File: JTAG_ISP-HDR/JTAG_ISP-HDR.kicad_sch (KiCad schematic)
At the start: 4 parts, among them J1 Conn_01x08, J2 Conn_01x08

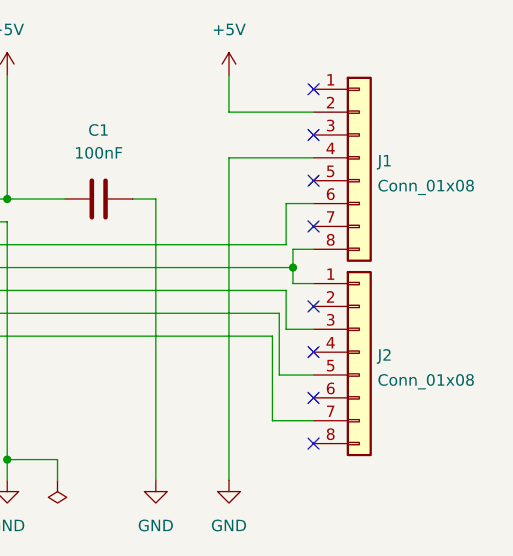
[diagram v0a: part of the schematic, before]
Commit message: # [PCB] ~ Modification du PCB pour le projet ISP en fonction des nouvelles connexions sur son schéma. + Ajout de trous aux 4 coins du PCB des 2 projets (ISP & HDR). ~ Augmentation de la taille du PCB des 2 projets en ajoutant 20mills en haut et en bas. ~ Diminution de l'espace de texte (nom et date).
# [SCHÉMA]
~ Modification du schéma pour le projet ISP basé sur le fil JTAG -> ISP déjà existant.
+ Ajout de texte sur le schéma des 2 projets indiquant le nom des broches sur les headers.
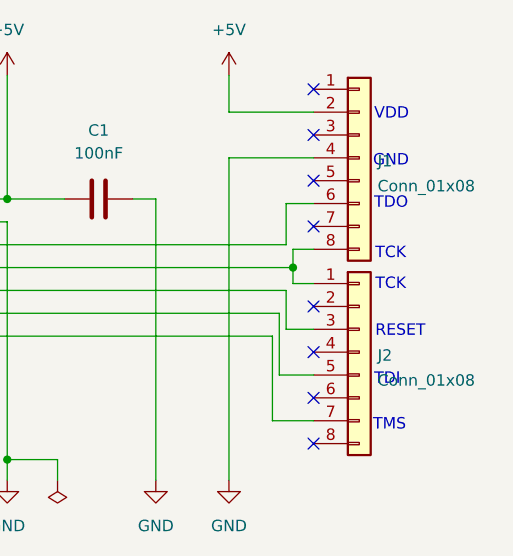
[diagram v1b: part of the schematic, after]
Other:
- note added: "GND"
- note added: "RESET"
- note added: "TCK"
- note added: "TDI"
- note added: "TDO"
- note added: "TMS"
- note added: "VDD"
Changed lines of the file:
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@@
     (stroke (width 0) (type default) (color 0 0 0 0))
+  )
+  (text "TDI" (at 181.483 108.712 0)
+    (effects (font (size 1.27 1.27)) (justify left bottom))
+  )
+  (text "TMS" (at 181.356 113.792 0)
+    (effects (font (size 1.27 1.27)) (justify left bottom))
+  )
+  (text "GND" (at 181.356 84.455 0)
+    (effects (font (size 1.27 1.27)) (justify left bottom))
+  )
+  (text "TCK" (at 181.61 94.742 0)
+    (effects (font (size 1.27 1.27)) (justify left bottom))
+  )
+  (text "TCK" (at 181.61 98.171 0)
+    (effects (font (size 1.27 1.27)) (justify left bottom))
+  )
+  (text "VDD" (at 181.483 79.248 0)
+    (effects (font (size 1.27 1.27)) (justify left bottom))
+  )
+  (text "RESET" (at 181.61 103.378 0)
+    (effects (font (size 1.27 1.27)) (justify left bottom))
+  )
+  (text "TDO" (at 181.483 89.154 0)
+    (effects (font (size 1.27 1.27)) (justify left bottom))
   )
   (symbol (lib_id "power:PWR_FLAG") (at 146.304 119.126 180) (unit 1)

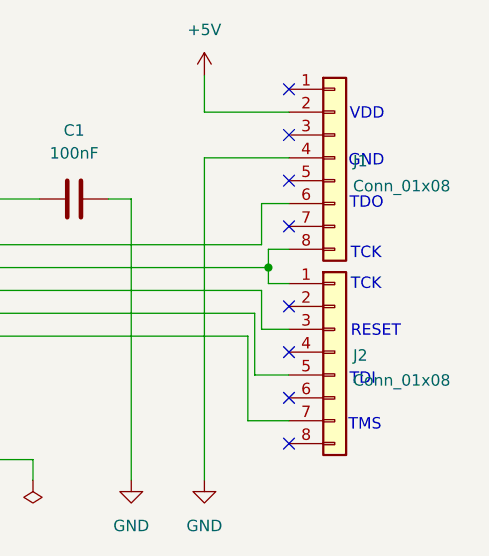
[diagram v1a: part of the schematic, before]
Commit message: # [PCB] ~ Modification du texte (date du jour) sur le PCB du projet HDR.
# [SCHÉMA]
~ Alignement du texte sur le schéma des 2 projets indiquant le nom des broches sur les headers.
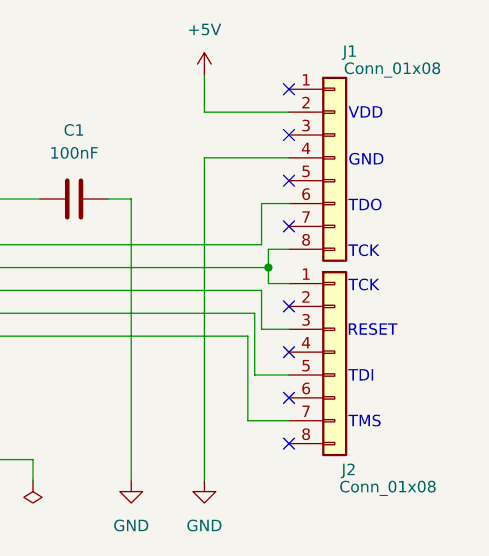
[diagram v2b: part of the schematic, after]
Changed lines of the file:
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@@
     (stroke (width 0) (type default) (color 0 0 0 0))
   )
-  (text "TDI" (at 181.483 108.712 0)
+  (text "TDI" (at 181.356 108.458 0)
     (effects (font (size 1.27 1.27)) (justify left bottom))
   )
-  (text "TMS" (at 181.356 113.792 0)
+  (text "TMS" (at 181.356 113.538 0)
     (effects (font (size 1.27 1.27)) (justify left bottom))
   )
@@
     (effects (font (size 1.27 1.27)) (justify left bottom))
   )
-  (text "TCK" (at 181.61 94.742 0)
+  (text "TCK" (at 181.356 94.615 0)
     (effects (font (size 1.27 1.27)) (justify left bottom))
   )
-  (text "TCK" (at 181.61 98.171 0)
+  (text "TCK" (at 181.356 98.425 0)
     (effects (font (size 1.27 1.27)) (justify left bottom))
   )
-  (text "VDD" (at 181.483 79.248 0)
+  (text "VDD" (at 181.356 79.248 0)
     (effects (font (size 1.27 1.27)) (justify left bottom))
   )
-  (text "RESET" (at 181.61 103.378 0)
+  (text "RESET" (at 181.229 103.378 0)
     (effects (font (size 1.27 1.27)) (justify left bottom))
   )
-  (text "TDO" (at 181.483 89.154 0)
+  (text "TDO" (at 181.356 89.535 0)
     (effects (font (size 1.27 1.27)) (justify left bottom))
   )
@@
   )
   (symbol (lib_id "Connector_Generic:Conn_01x08") (at 179.832 83.312 0) (unit 1)
-    (in_bom yes) (on_board yes) (fields_autoplaced)
-    (property "Reference" "J1" (id 0) (at 181.864 83.6735 0)
+    (in_bom yes) (on_board yes)
+    (property "Reference" "J1" (id 0) (at 180.721 71.501 0)
       (effects (font (size 1.27 1.27)) (justify left))
     )
-    (property "Value" "Conn_01x08" (id 1) (at 181.864 86.4486 0)
+    (property "Value" "Conn_01x08" (id 1) (at 180.848 73.406 0)
       (effects (font (size 1.27 1.27)) (justify left))
     )
@@
   )
   (symbol (lib_id "Connector_Generic:Conn_01x08") (at 179.832 104.902 0) (unit 1)
-    (in_bom yes) (on_board yes) (fields_autoplaced)
-    (property "Reference" "J2" (id 0) (at 181.864 105.2635 0)
+    (in_bom yes) (on_board yes)
+    (property "Reference" "J2" (id 0) (at 180.594 117.983 0)
       (effects (font (size 1.27 1.27)) (justify left))
     )
-    (property "Value" "Conn_01x08" (id 1) (at 181.864 108.0386 0)
+    (property "Value" "Conn_01x08" (id 1) (at 180.34 119.888 0)
       (effects (font (size 1.27 1.27)) (justify left))
     )

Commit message: # [PCB] + Ajout d'un encavure dans le haut du PCB du projet HDR pour que la dragone ne dépasse pas sur le bord du PCB. - Suppression du fichier .round-tracks-config qui est inutile. * Mise à jours de la cartouche pour les 2 projets.     * Date actuelle.     * Version actuelle.     * Titre du projet.
# [SCHÉMA]
* Mise à jours de la cartouche pour les 2 projets.
    * Date actuelle.
    * Version actuelle.
    * Titre du projet.
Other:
- title: JTAG_ISP -> JTAG_ISP / HDR
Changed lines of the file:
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@@
   (paper "A4")
   (title_block
-    (title "JTAG_ISP")
-    (date "2022-03-12")
-    (rev "v1.0.0")
+    (title "JTAG_ISP / HDR")
+    (date "2022-03-17")
+    (rev "v4.1.0")
   )
   (junction (at 172.466 95.504) (diameter 0) (color 0 0 0 0)

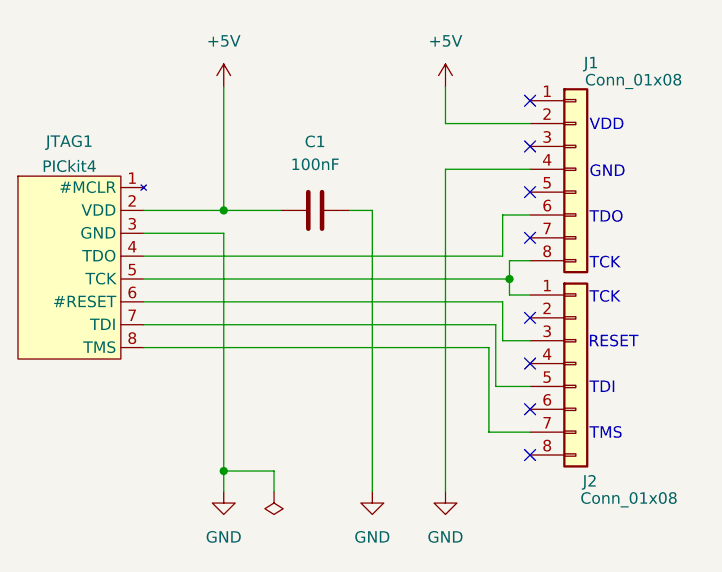
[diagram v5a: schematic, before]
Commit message: # [PCB] + Ajout de GND et de VCC dans le projet HDR sur les broches non utilisés de J1 & J2.     + Ajout des nouveaux vias. * Projet HDR routé à nouveau. * Utilisation de trous de montage avec pads. * Flèche d'indication de la broche #1 pour le PICKit4 dans le projet HDR est déplacée pour s'alligner avec celle sur le PICKit4. * Modification du texte (initiales et date du jour) sur le PCB du projet HDR.
# [SCHÉMA]
+ Ajout de GND et de VCC dans le projet HDR sur les broches non utilisées de J1 & J2.
    + Ajout des nouveaux noms de broches sur J1 & J2.
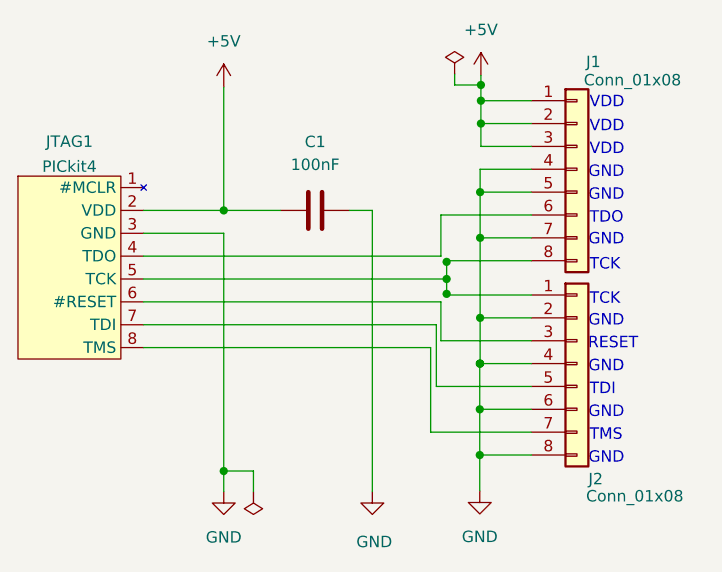
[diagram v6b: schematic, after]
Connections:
- net +5V: now also J1.1 (Pin_1), J1.3 (Pin_3)
- net GND: now also J1.5 (Pin_5), J1.7 (Pin_7), J2.2 (Pin_2), J2.4 (Pin_4), J2.6 (Pin_6), J2.8 (Pin_8)
- no-connect marks 8 -> 0

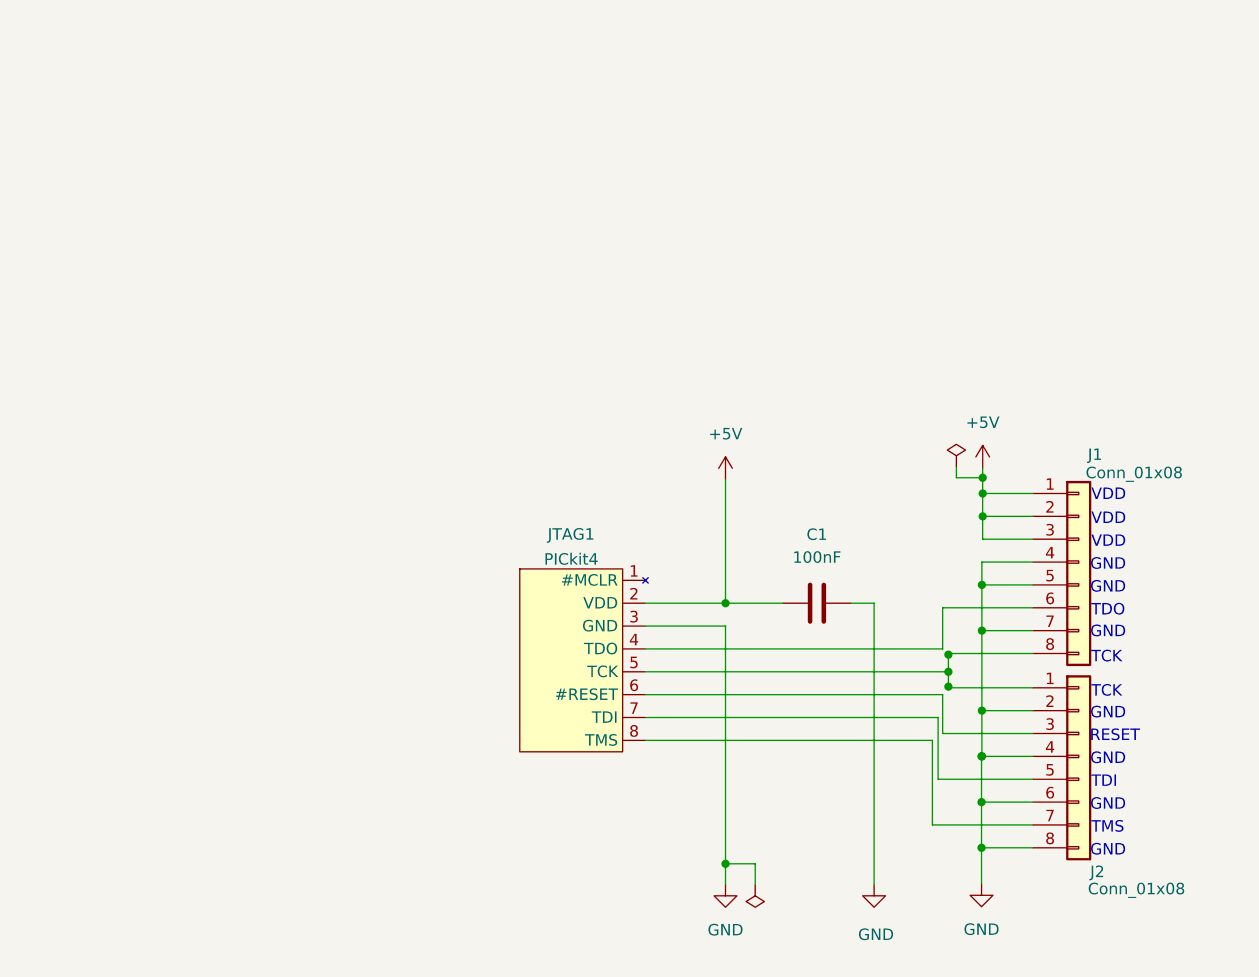
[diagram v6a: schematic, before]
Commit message: # Version compacte en cours... ## Les headers passent à travers d'un PCB et dépassent moins que la version précédente.
# [PCB]
+ Ajout d'un trou pour l'ISP dans le PCB du projet HDR.
+ Ajout d'un trou pour le PICkit dans le PCB du projet ISP.
* Déplacement du circuit de DEL dans le projet HDR.
* Projet ISP routé à nouveau.
* Mise à jour de la cartouche pour les 2 projets.
    * Date actuelle;
    * Version actuelle;

# [SCHÉMA]
+ Ajout d'encadrés pointillés dan les 2 projets pour séparer les parties du schémas.
* Déplacement du circuit de DEL dans le projet HDR.
* Réduction de la valeur de la résistance pour le circuit de DEL.
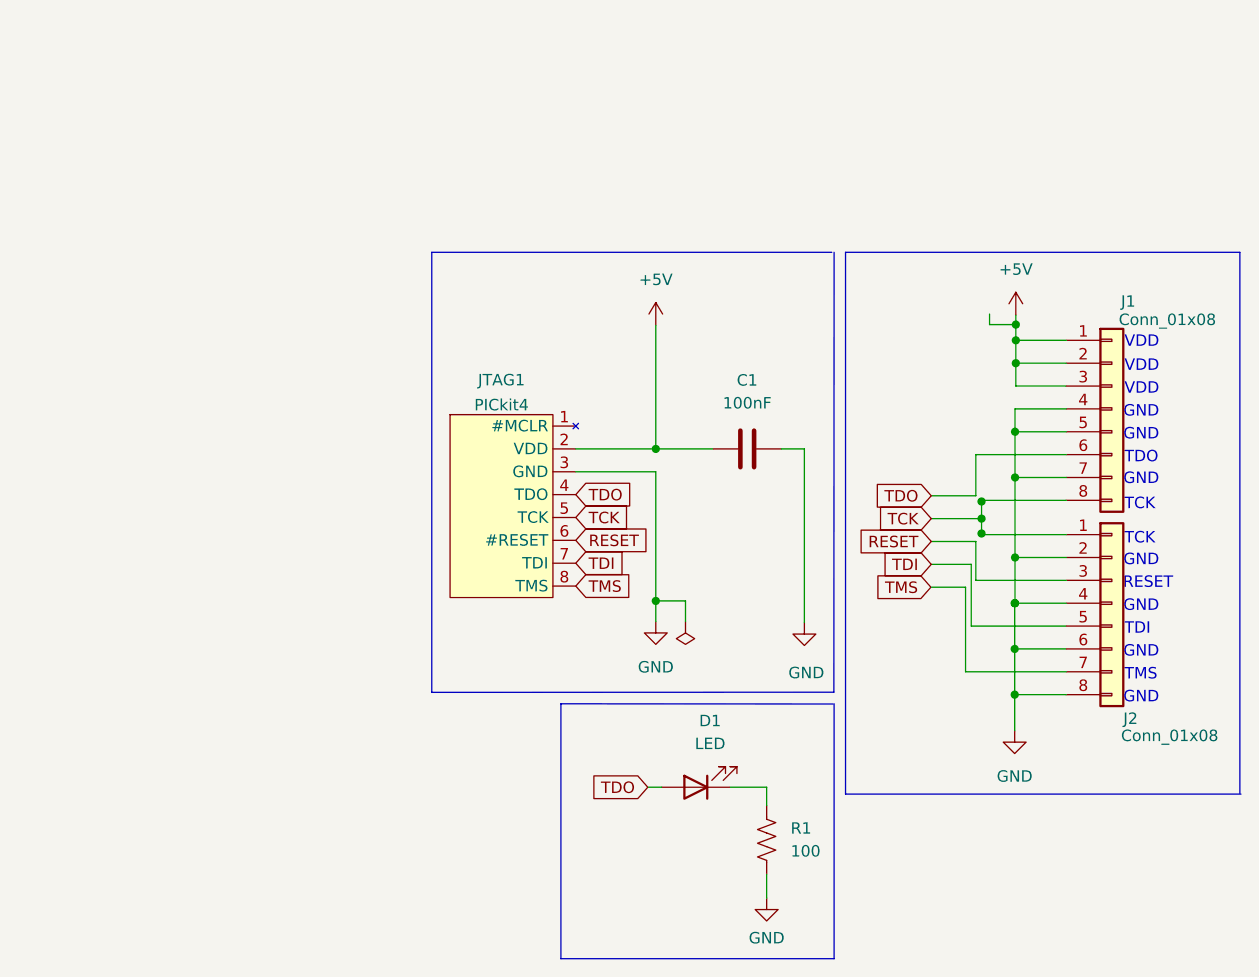
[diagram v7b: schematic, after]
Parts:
- added D1: LED, LED_THT:LED_D3.0mm, symbol Device:LED
- added R1: 100, Resistor_THT:R_Axial_DIN0207_L6.3mm_D2.5mm_P10.16mm_Horizontal, symbol Device:R_US
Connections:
- net GND: now also R1.2
- net TDO: now reaches J1.6 (Pin_6), JTAG1.4 (TDO)
- net TDO: now also D1.2 (A)
- net TCK: now reaches J1.8 (Pin_8), J2.1 (Pin_1), JTAG1.5 (TCK)
- net RESET: now reaches J2.3 (Pin_3), JTAG1.6 (#RESET)
- net TDI: now reaches J2.5 (Pin_5), JTAG1.7 (TDI)
- net TMS: now reaches J2.7 (Pin_7), JTAG1.8 (TMS)
- new net: D1.1 (K), R1.1
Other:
- moved on the sheet: J1, J2

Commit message: # [PCB] + Ajout du dégagement de 40 mils sur la bordure du trou au centre du PCB et sur le pourtour. + Ajout de la flèche indiquand la broche #1 du header du ISP. + Double vias pour les traces d'alimentation. - Suppression du texte (date du jour) dans le bas du PCB. - Suppression de la flèche indiquand la broche #1 du header PICkit4. * Nouveau format de page A5. * PCB routé à nouveau. * Mise à jour de la cartouche.     * Date actuelle;     * Version actuelle.
# [SCHÉMA]
* Mise à jour de la cartouche.
    * Date actuelle;
    * Version actuelle.
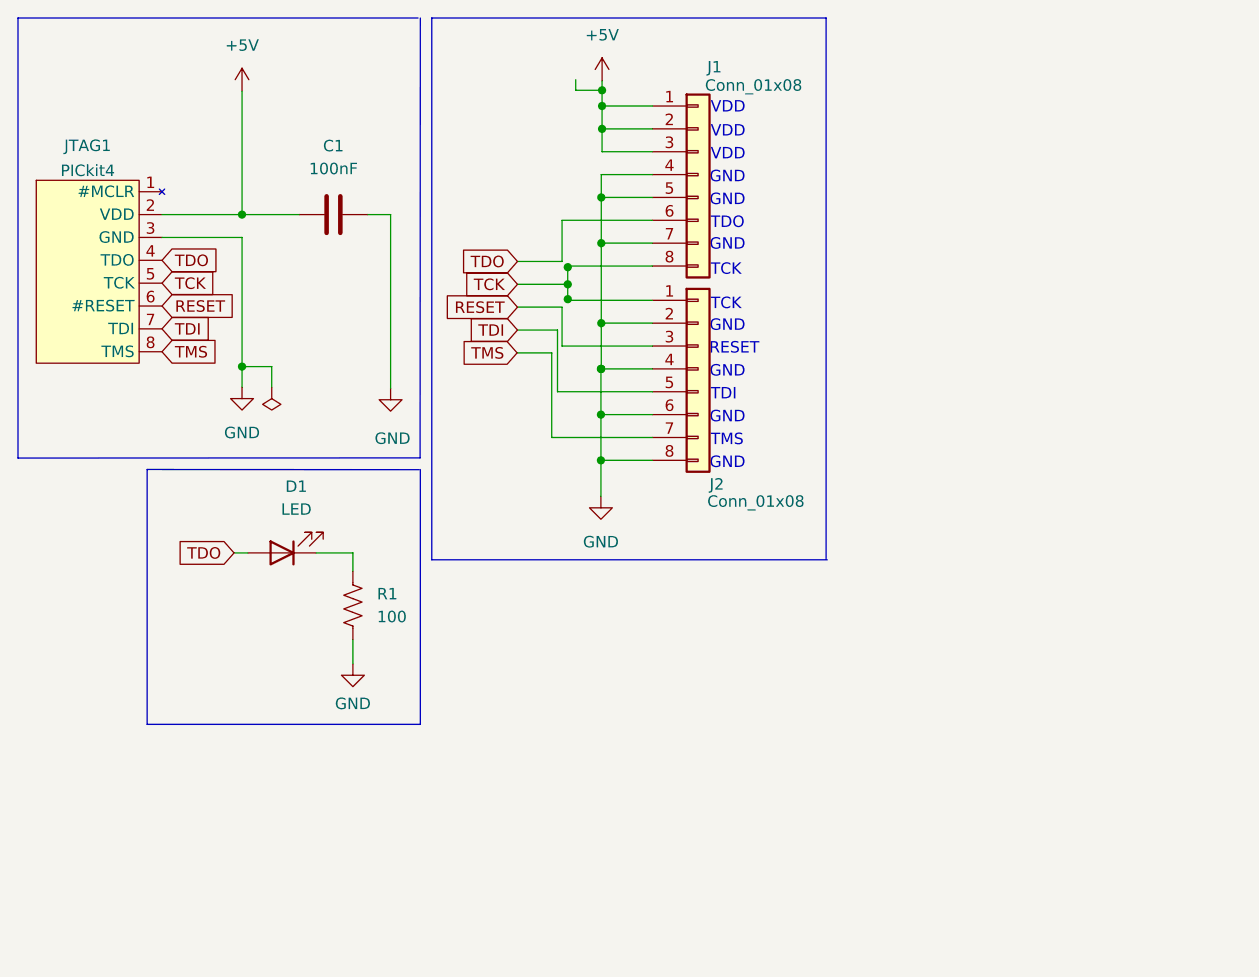
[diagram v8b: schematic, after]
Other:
- moved on the sheet: C1, D1, J1, J2, JTAG1, R1
